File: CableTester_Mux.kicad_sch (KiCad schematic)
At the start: 76 parts, among them J1 MircoMatch, J2 MircoMatch, J3 MircoMatch, J4 MircoMatch, J5 1787072, J6 SMB, J7 Keystone 7792, J8 Keystone 7792, U1 DG1206EUI+

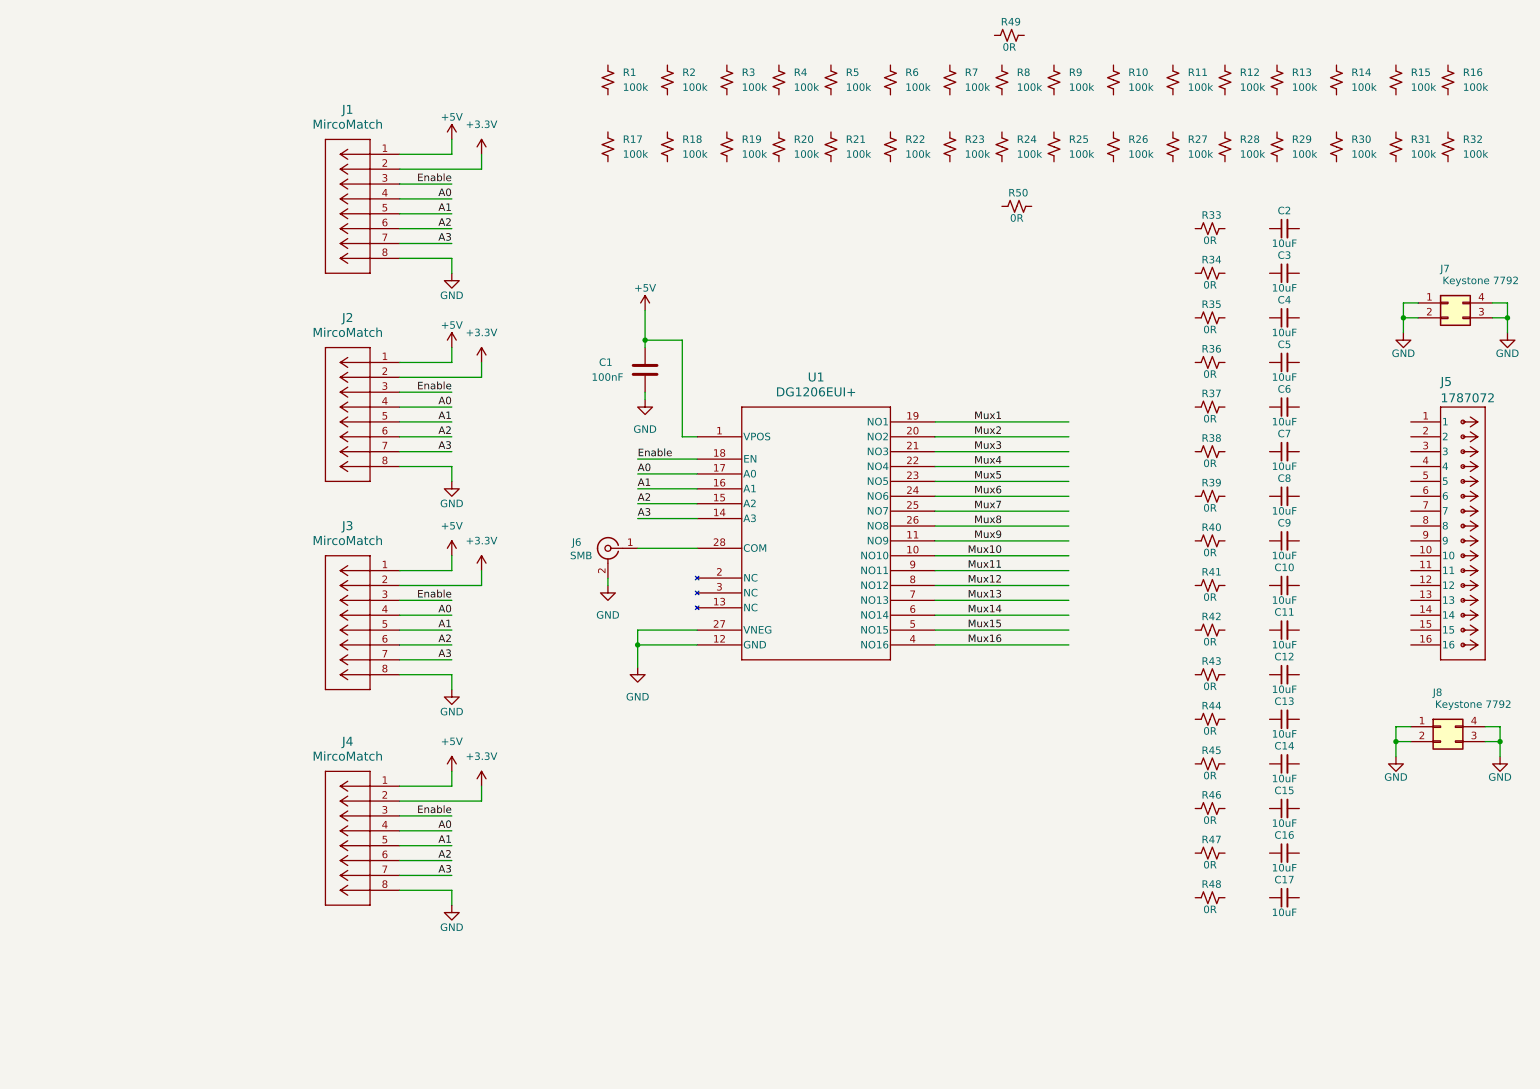
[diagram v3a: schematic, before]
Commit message: Updated Schematics with filter for AC UART signaling
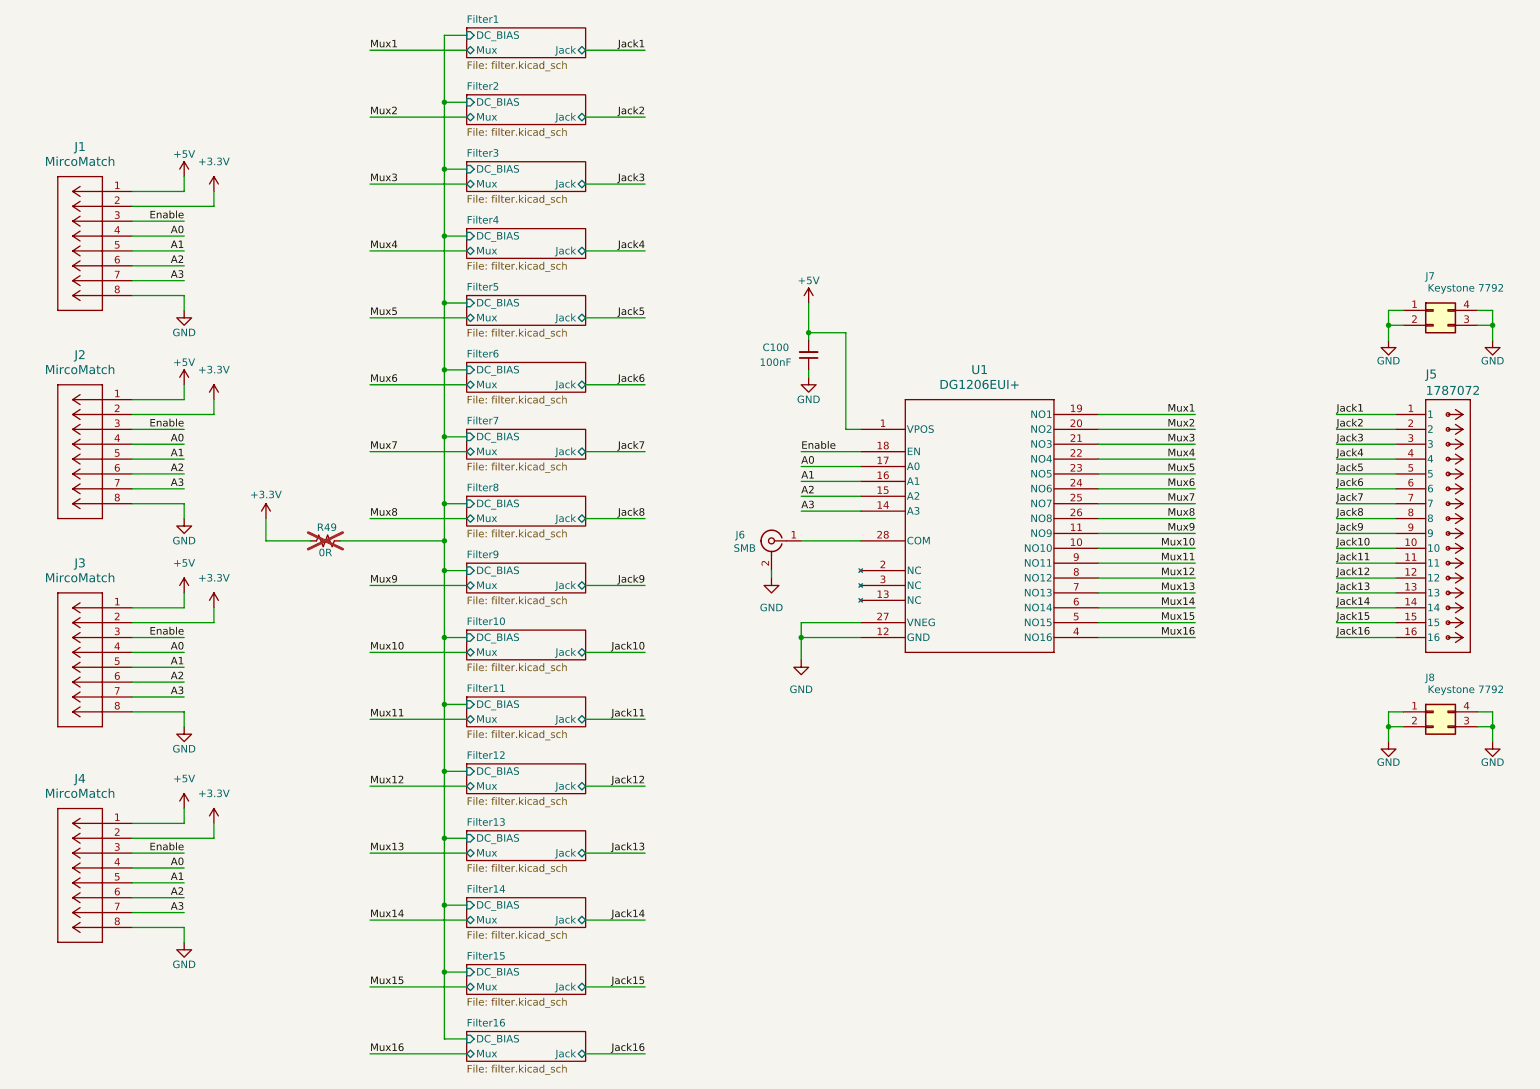
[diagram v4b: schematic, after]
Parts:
- removed C10, C11, C12, C13, C14, C15, C16, C17, C2, C3, C4, C5, C6, C7, C8, C9: 10uF, Capacitor_SMD:C_1210_3225Metric_Pad1.33x2.70mm_HandSolder, symbol Device:C_Small
- removed R1, R10, R11, R12, R13, R14, R15, R16, R17, R18, R19, R2, R20, R21, R22, R23, R24, R25, R26, R27, R28, R29, R3, R30, R31, R32, R4, R5, R6, R7, R8, R9: 100k, Resistor_SMD:R_0603_1608Metric_Pad0.98x0.95mm_HandSolder, symbol Device:R_Small_US
- removed R33, R34, R35, R36, R37, R38, R39, R40, R41, R42, R43, R44, R45, R46, R47, R48, R50: 0R, Resistor_SMD:R_0603_1608Metric_Pad0.98x0.95mm_HandSolder, symbol Device:R_Small_US
- C100: renamed from C1; symbol Device:C -> Device:C_Small
- R49: now not fitted; now left out of the parts list
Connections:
- net +3.3V: now also R49.1
- net Jack1: now reaches J5.1
- net Jack10: now reaches J5.10
- net Jack11: now reaches J5.11
- net Jack12: now reaches J5.12
- net Jack13: now reaches J5.13
- net Jack14: now reaches J5.14
- net Jack15: now reaches J5.15
- net Jack16: now reaches J5.16
- net Jack2: now reaches J5.2
- net Jack3: now reaches J5.3
- net Jack4: now reaches J5.4
- net Jack5: now reaches J5.5
- net Jack6: now reaches J5.6
- net Jack7: now reaches J5.7
- net Jack8: now reaches J5.8
- net Jack9: now reaches J5.9
- net Filter1/DC_BIAS: now reaches R49.2
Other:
- added sheet Filter1 (filter.kicad_sch)
- added sheet Filter10 (filter.kicad_sch)
- added sheet Filter11 (filter.kicad_sch)
- added sheet Filter12 (filter.kicad_sch)
- added sheet Filter13 (filter.kicad_sch)
- added sheet Filter14 (filter.kicad_sch)
- added sheet Filter15 (filter.kicad_sch)
- added sheet Filter16 (filter.kicad_sch)
- added sheet Filter2 (filter.kicad_sch)
- added sheet Filter3 (filter.kicad_sch)
- added sheet Filter4 (filter.kicad_sch)
- added sheet Filter5 (filter.kicad_sch)
- added sheet Filter6 (filter.kicad_sch)
- added sheet Filter7 (filter.kicad_sch)
- added sheet Filter8 (filter.kicad_sch)
- added sheet Filter9 (filter.kicad_sch)
- moved on the sheet: C100, J1, J2, J3, J4, J5, J6, J7, J8, U1

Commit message: Removed DC-Blocking filter and update schmatic and layout
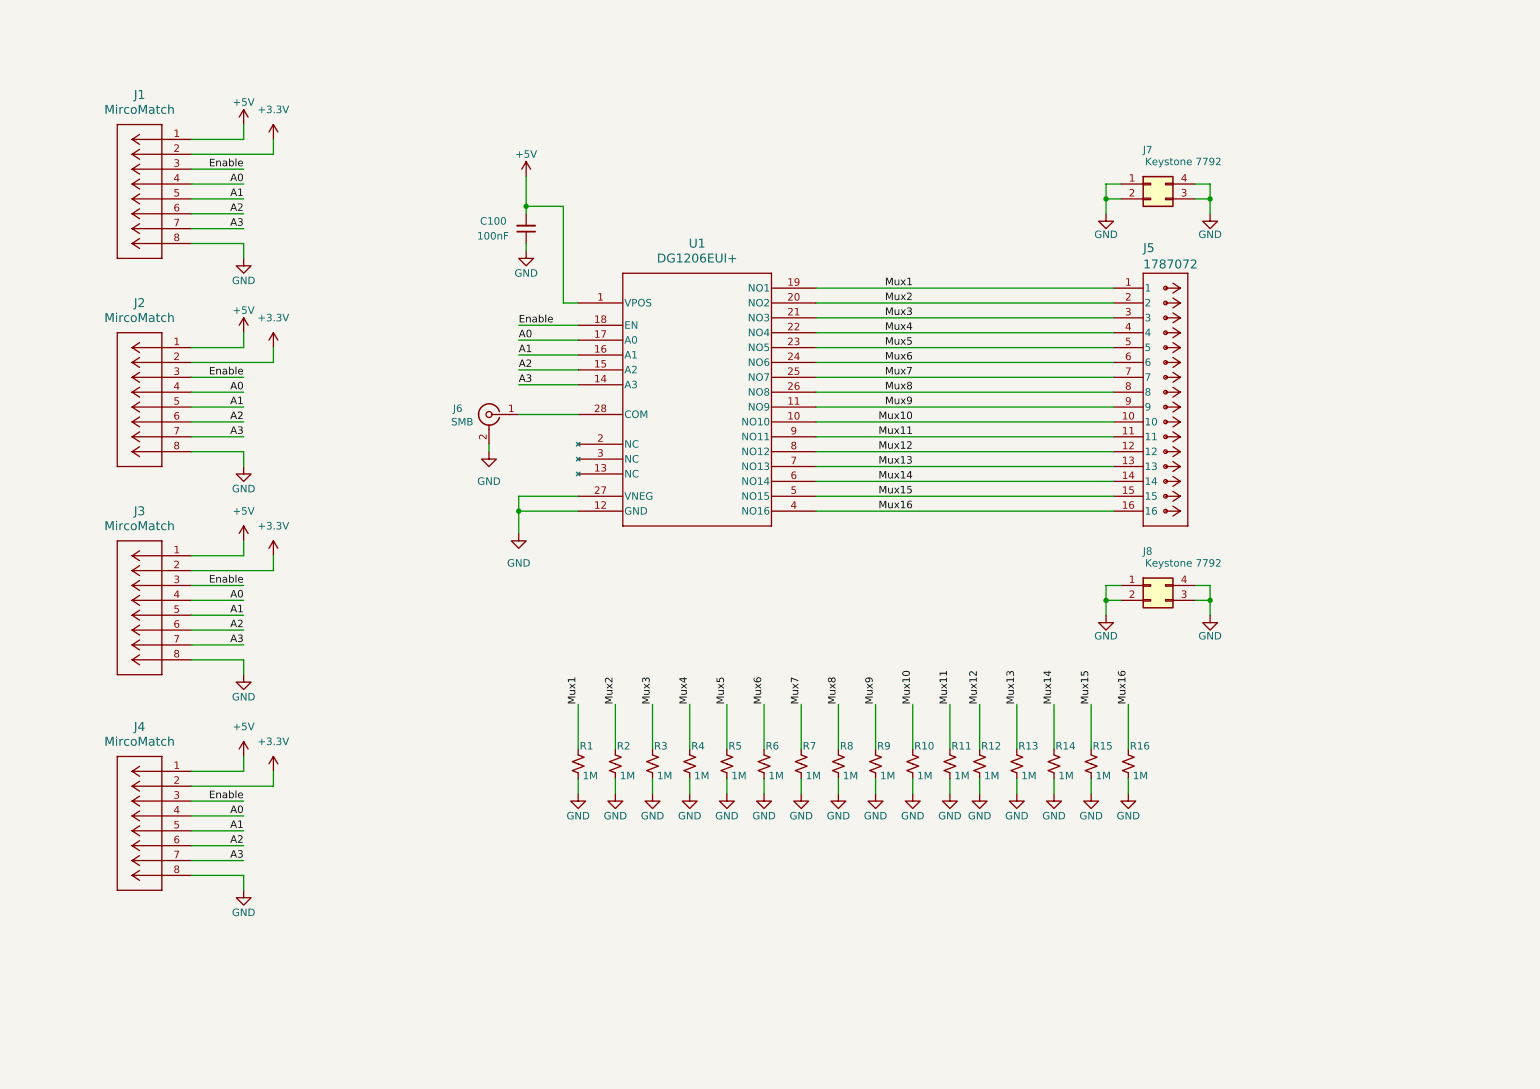
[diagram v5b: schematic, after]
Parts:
- removed R49: 0R, Resistor_SMD:R_0603_1608Metric_Pad0.98x0.95mm_HandSolder, symbol Device:R_Small_US
- added R1, R10, R11, R12, R13, R14, R15, R16, R2, R3, R4, R5, R6, R7, R8, R9: 1M, Resistor_SMD:R_0603_1608Metric_Pad0.98x0.95mm_HandSolder, symbol Device:R_Small_US
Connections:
- net Jack1 is gone; now on net Mux1: J5.1
- net Jack10 is gone; now on net Mux10: J5.10
- net Jack11 is gone; now on net Mux11: J5.11
- net Jack12 is gone; now on net Mux12: J5.12
- net Jack13 is gone; now on net Mux13: J5.13
- net Jack14 is gone; now on net Mux14: J5.14
- net Jack15 is gone; now on net Mux15: J5.15
- net Jack16 is gone; now on net Mux16: J5.16
- net Jack2 is gone; now on net Mux2: J5.2
- net Jack3 is gone; now on net Mux3: J5.3
- net Jack4 is gone; now on net Mux4: J5.4
- net Jack5 is gone; now on net Mux5: J5.5
- net Jack6 is gone; now on net Mux6: J5.6
- net Jack7 is gone; now on net Mux7: J5.7
- net Jack8 is gone; now on net Mux8: J5.8
- net Jack9 is gone; now on net Mux9: J5.9
- net GND: now also R1.2, R10.2, R11.2, R12.2, R13.2, R14.2, R15.2, R16.2, R2.2, R3.2, R4.2, R5.2, R6.2, R7.2, R8.2, R9.2
- net Mux1: now also R1.1
- net Mux10: now also R10.1
- net Mux11: now also R11.1
- net Mux12: now also R12.1
- net Mux13: now also R13.1
- net Mux14: now also R14.1
- net Mux15: now also R15.1
- net Mux16: now also R16.1
- net Mux2: now also R2.1
- net Mux3: now also R3.1
- net Mux4: now also R4.1
- net Mux5: now also R5.1
- net Mux6: now also R6.1
- net Mux7: now also R7.1
- net Mux8: now also R8.1
- net Mux9: now also R9.1
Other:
- removed sheet Filter1
- removed sheet Filter10
- removed sheet Filter11
- removed sheet Filter12
- removed sheet Filter13
- removed sheet Filter14
- removed sheet Filter15
- removed sheet Filter16
- removed sheet Filter2
- removed sheet Filter3
- removed sheet Filter4
- removed sheet Filter5
- removed sheet Filter6
- removed sheet Filter7
- removed sheet Filter8
- removed sheet Filter9
- moved on the sheet: C100, J1, J2, J3, J4, J5, J6, J7, J8, U1
